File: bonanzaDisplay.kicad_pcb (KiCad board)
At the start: 6 copper layers, 76 x 101 mm, 71 parts, among them J1 OLED-1.31-SSD1322, J15 SWD, J5 Conn_01x10, J6 USB_C_Receptacle_USB2.0, SW1 TS-1088-AR02016, SW2 TS-1088-AR02016, SW3 SIQ-02FVS3_C41430892, U1 RP2354A, U10 TPS82130, U2 XC6206P302MR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

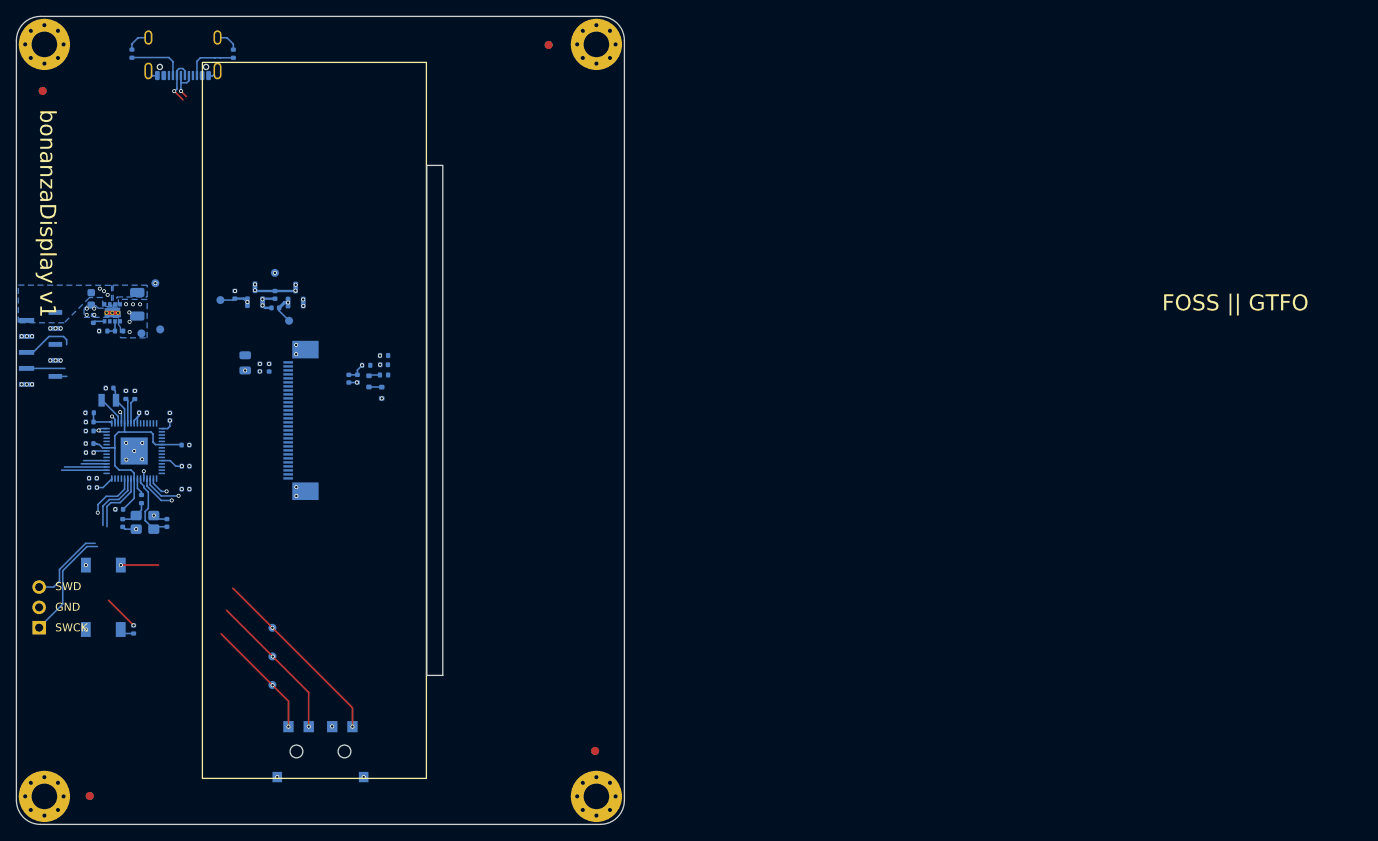
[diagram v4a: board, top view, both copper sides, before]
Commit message: switched 10pin FFC connector to right angle. made PCB shorter. most routing done.
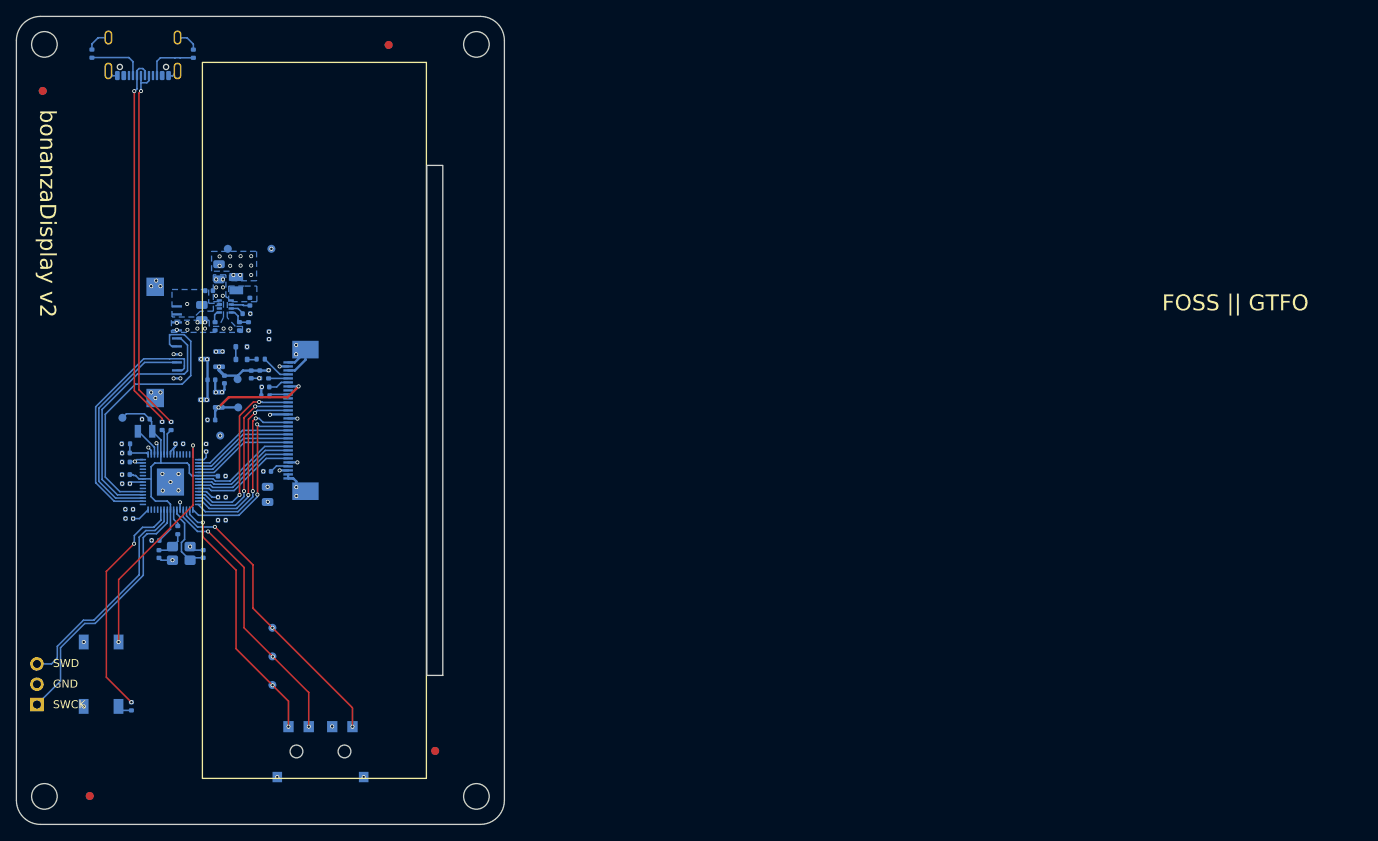
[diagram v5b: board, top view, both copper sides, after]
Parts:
- removed U10: TPS82130, bonanzaDisplay:Texas_SIL0008D_MicroSiP-8-1EP_2.8x3mm_P0.65mm_EP1.1x1.9mm_ThermalVias
- added C37: 0.1uF, Capacitor_SMD:C_0402_1005Metric, B.Cu at (124.1, 73.3)
- added C41: 0.1uF, Capacitor_SMD:C_0402_1005Metric, B.Cu at (129.2, 74.7)
- added L2: 1.5uH, bonanzaDisplay:IND-SMD_L2.0-W1.6, B.Cu at (127.5, 72.4)
- added R14: 13.7k, Resistor_SMD:R_0402_1005Metric, B.Cu at (124.8, 77.7)
- added U4: TPS62933DRLR, bonanzaDisplay:SOT-583-8_L2.1-W1.2-P0.50-LS1.6-BR, B.Cu at (126.1, 75.3)
- C29: value 3.3nF -> 33nF
- C34: footprint Capacitor_SMD:C_1206_3216Metric -> Capacitor_SMD:C_0805_2012Metric
- C8: footprint Capacitor_SMD:C_0603_1608Metric -> Capacitor_SMD:C_0805_2012Metric
- H1, H2, H3, H4: footprint MountingHole:MountingHole_3.2mm_M3_Pad_Via -> MountingHole:MountingHole_3.2mm_M3
- J5: footprint bonanzaDisplay:CONN10_1-1735042-0 -> bonanzaDisplay:FPC-SMD_10P-P1.0_FGS-XJ-H2.0
- R12: value 309k -> 30.9k
- R13: value 100k -> 10k
- moved TP18 21.5 mm to (125.5, 91.4), turned to -90 degrees
- moved FID2 20.0 mm to (146.5, 42.6)
- moved FID3 20.0 mm to (152.3, 130.8)
- moved C29 19.2 mm to (128.8, 76.2), turned to 180 degrees
- moved D2 18.5 mm to (128.1, 80.3), turned to 180 degrees
- moved R13 17.0 mm to (127.9, 77.7), turned to 90 degrees
- moved C36 16.7 mm to (131.4, 98.8), turned to -90 degrees
- moved R12 16.2 mm to (129.0, 77.7), turned to -90 degrees
- moved D3 16.2 mm to (128.1, 81.9), turned to 0 degrees
- moved C40 15.9 mm to (124.4, 89.4), turned to 180 degrees
- moved J5 15.7 mm to (118.7, 79.8)
- moved R35 15.7 mm to (131.1, 86.4)
- moved R34 15.5 mm to (130.5, 81.8)
- moved TP19 15.1 mm to (131.9, 68.0)
- moved TP9 15.1 mm to (126.4, 68.0)
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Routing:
- net /USB_DP: track 4.91 -> 47.1 mm
- net /USB_DN: track 6.21 -> 47.5 mm
- net /DISP_GPIO1: track 3.83 -> 32.2 mm
- net /DISP_GPIO2: track 9.47 -> 35.5 mm
- net /DISP_SDA: track 7.03 -> 32.1 mm
- net Net-(U1-~{QSPI_SS}): track 4.72 -> 29.6 mm, vias 1 -> 2
- net /RES: track 0.00 -> 22.6 mm, vias 0 -> 2
- net /CS: track 0.00 -> 22.5 mm, vias 0 -> 2
- net /DC: track 0.00 -> 22.4 mm, vias 0 -> 2
- net /E/RD: track 0.00 -> 22.4 mm, vias 0 -> 2
- net /R/W: track 0.00 -> 22.2 mm, vias 0 -> 2
- net Net-(U1-RUN): track 10.9 -> 29.0 mm
- net /DISP_SCL: track 10.0 -> 27.6 mm
- net /SW_CCW: track 17.7 -> 32.6 mm
- net /2V8: track 3.65 -> 16.9 mm, vias 1 -> 2
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- added copper zone on B.Cu, net Net-(U4-SW)
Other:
- board size 76 x 101 mm -> 61 x 101 mm
- board text added: "bonanzaDisplay v2"
- board text removed: "bonanzaDisplay v1"

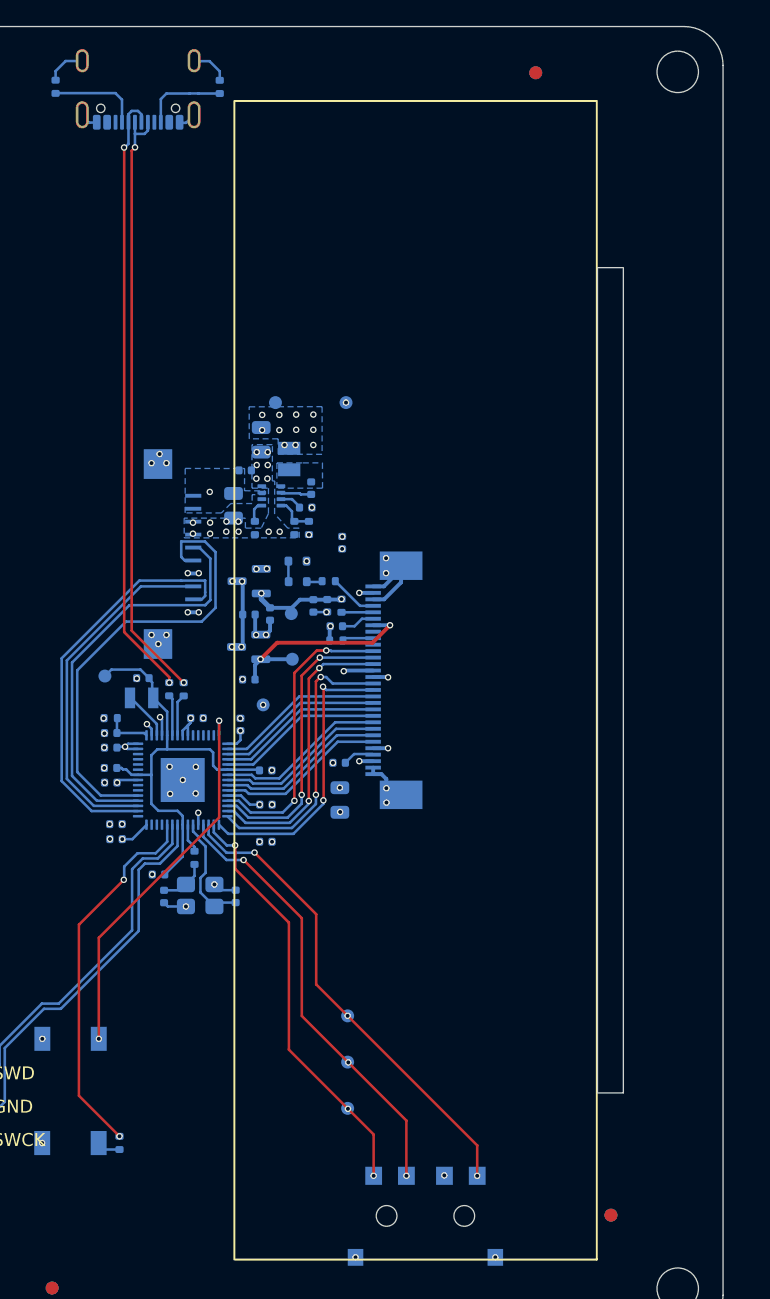
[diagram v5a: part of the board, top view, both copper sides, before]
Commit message: cleanup footprints
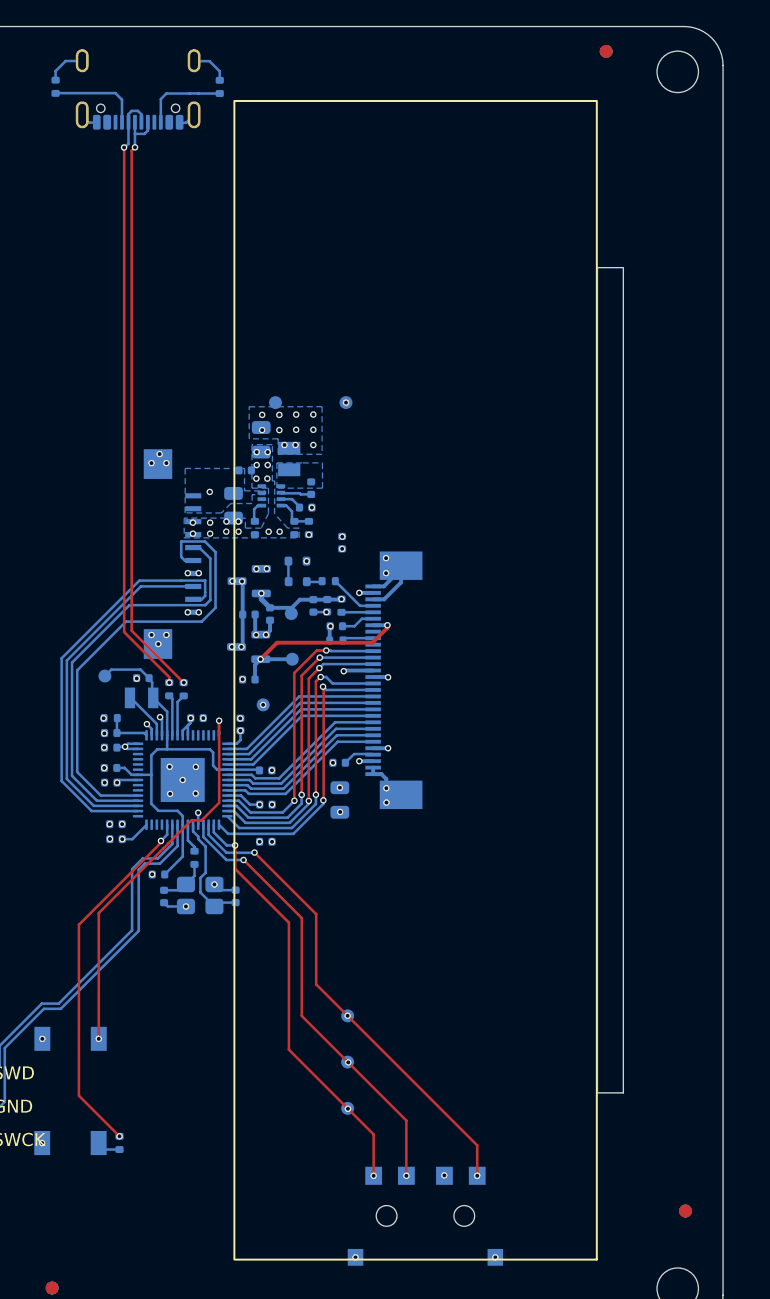
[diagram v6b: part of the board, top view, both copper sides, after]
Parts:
- moved FID3 5.77 mm to (158.1, 130.5)
- moved FID2 5.69 mm to (152.0, 40.9)
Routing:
- net Net-(U1-RUN): track 29.0 -> 28.2 mm

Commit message: DRC pass, updated BOM
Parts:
- SW3: value SIQ-02FVS3_C41430892 -> SIQ-02FVS3
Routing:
- net /DISP_GPIO2: track 35.5 -> 27.5 mm
- net /DISP_GPIO1: track 32.2 -> 29.8 mm
- net /DISP_SDA: track 32.1 -> 30.1 mm, vias 0 -> 2
- net Net-(J1-VSL): track 3.72 -> 4.31 mm
- net /DISP_SCL: vias 0 -> 2
- net /3V0: vias 3 -> 2
